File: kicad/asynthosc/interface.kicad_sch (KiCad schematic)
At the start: 22 parts, among them SW6 RotaryEncoder_Switch, SW7 SW_MEC_5G_LED, SW8 SW_MEC_5G_LED

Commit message: bom: adding jlc ref to generic
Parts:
- C51, C52: LCSC (none) -> C307331
- C53: LCSC (none) -> C377773
- C54, C55: LCSC (none) -> C28323
- C56: LCSC (none) -> C1779
- C57: LCSC (none) -> C49678
- R76, R77, R78, R79, R84: LCSC (none) -> C25744
- R80, R81: LCSC (none) -> C144055
- R82: LCSC (none) -> C26083
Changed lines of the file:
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@@
 			)
 		)
-		(property "LCSC" ""
+		(property "LCSC" "C1779"
 			(at 191.77 34.29 0)
 			(effects
@@
 			)
 		)
-		(property "LCSC" ""
+		(property "LCSC" "C307331"
 			(at 36.83 134.62 0)
 			(effects
@@
 			)
 		)
-		(property "LCSC" ""
+		(property "LCSC" "C49678"
 			(at 204.47 34.29 0)
 			(effects
@@
 			)
 		)
-		(property "LCSC" ""
+		(property "LCSC" "C28323"
 			(at 167.64 34.29 0)
 			(effects
@@
 			)
 		)
-		(property "LCSC" ""
+		(property "LCSC" "C25744"
 			(at 50.8 67.31 0)
 			(effects
@@
 			)
 		)
-		(property "LCSC" ""
+		(property "LCSC" "C377773"
 			(at 151.13 128.27 0)
 			(effects
@@
 			)
 		)
-		(property "LCSC" ""
+		(property "LCSC" "C25744"
 			(at 36.83 114.3 0)
 			(effects
@@
 			)
 		)
-		(property "LCSC" ""
+		(property "LCSC" "C25744"
 			(at 44.45 114.3 0)
 			(effects
@@
 			)
 		)
-		(property "LCSC" ""
+		(property "LCSC" "C25744"
 			(at 78.74 134.62 0)
 			(effects
@@
 			)
 		)
-		(property "LCSC" ""
+		(property "LCSC" "C144055"
 			(at 78.74 176.53 0)
 			(effects
@@
 			)
 		)
-		(property "LCSC" ""
+		(property "LCSC" "C25744"
 			(at 52.07 168.91 0)
 			(effects
@@
 			)
 		)
-		(property "LCSC" ""
+		(property "LCSC" "C26083"
 			(at 137.16 125.73 0)
 			(effects
@@
 			)
 		)
-		(property "LCSC" ""
+		(property "LCSC" "C28323"
 			(at 158.75 34.29 0)
 			(effects
@@
 			)
 		)
-		(property "LCSC" ""
+		(property "LCSC" "C307331"
 			(at 44.45 134.62 0)
 			(effects
@@
 			)
 		)
-		(property "LCSC" ""
+		(property "LCSC" "C144055"
 			(at 77.47 74.93 0)
 			(effects

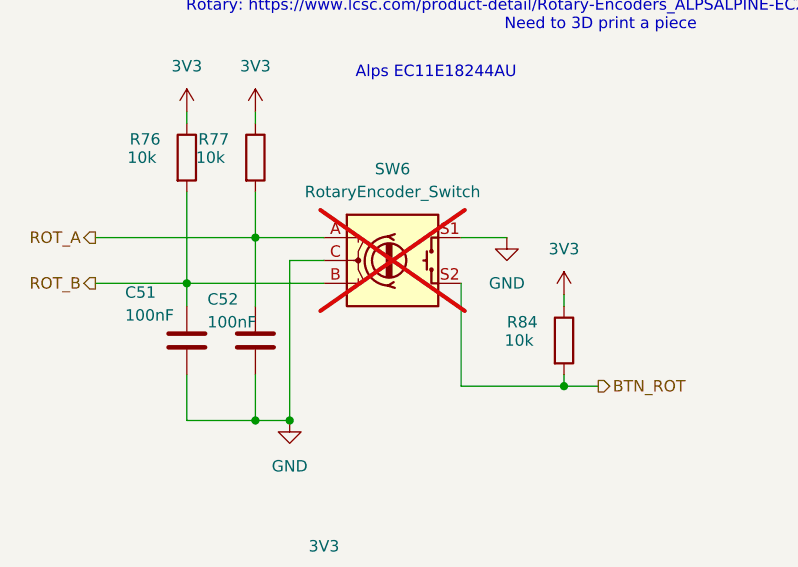
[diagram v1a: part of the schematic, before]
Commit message: sch: bom: fix footprints and bom
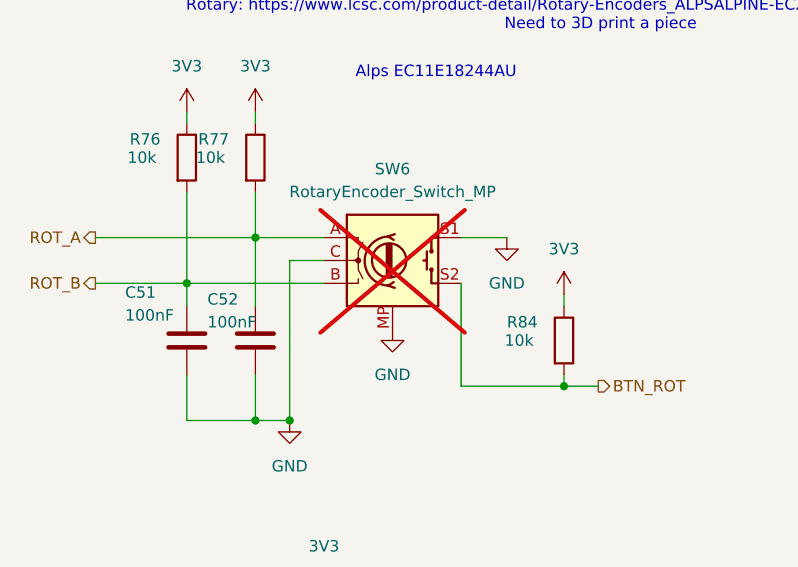
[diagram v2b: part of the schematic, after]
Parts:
- DS1: footprint asynthosc:Hirose_FH52-24S-0.5SH_1x24-1MP_P0.5mm_Horizontal -> Display:OLED-128O064D
- SW6: value RotaryEncoder_Switch -> RotaryEncoder_Switch_MP; symbol Device:RotaryEncoder_Switch -> Device:RotaryEncoder_Switch_MP
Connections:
- net GND: now also SW6.MP
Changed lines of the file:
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@@
 			)
 		)
-		(property "Footprint" "asynthosc:Hirose_FH52-24S-0.5SH_1x24-1MP_P0.5mm_Horizontal"
+		(property "Footprint" "Display:OLED-128O064D"
 			(at 183.642 96.774 0)
 			(effects
@@
 	)
 	(symbol
+		(lib_id "power:GND")
+		(at 59.69 133.35 0)
+		(unit 1)
+		(exclude_from_sim no)
+		(in_bom yes)
+		(on_board yes)
+		(dnp no)
+		(fields_autoplaced yes)
+		(property "Reference" "#PWR0162"
+			(at 59.69 139.7 0)
+			(effects
+				(font
+					(size 1.27 1.27)
+				)
+				(hide yes)
+			)
+		)
+		(property "Value" "GND"
+			(at 59.69 138.43 0)
+			(effects
+				(font
+					(size 1.27 1.27)
+				)
+			)
+		)
+		(property "Footprint" ""
+			(at 59.69 133.35 0)
+			(effects
+				(font
+					(size 1.27 1.27)
+				)
+				(hide yes)
+			)
+		)
+		(property "Datasheet" ""
+			(at 59.69 133.35 0)
+			(effects
+				(font
+					(size 1.27 1.27)
+				)
+				(hide yes)
+			)
+		)
+		(property "Description" "Power symbol creates a global label with name \"GND\" , ground"
+			(at 59.69 133.35 0)
+			(effects
+				(font
+					(size 1.27 1.27)
+				)
+				(hide yes)
+			)
+		)
+		(pin "1"
+		)
+		(instances
+			(project "asynthosc"
+				(path "/d73e377a-a016-415f-8824-91cc6e4907b9/b863f609-74bc-4dca-9f89-b76b25b90e2d"
+					(reference "#PWR0162")
+					(unit 1)
+				)
+			)
+		)
+	)
+	(symbol
 		(lib_id "power:+3V3")
 		(at 50.8 60.96 0)
@@
 	)
 	(symbol
-		(lib_id "Device:RotaryEncoder_Switch")
+		(lib_id "Device:RotaryEncoder_Switch_MP")
 		(at 59.69 125.73 0)
 		(unit 1)
@@
 			)
 		)
-		(property "Value" "RotaryEncoder_Switch"
+		(property "Value" "RotaryEncoder_Switch_MP"
 			(at 59.69 118.11 0)
 			(effects
@@
 		)
 		(property "Datasheet" "~"
-			(at 59.69 119.126 0)
-			(effects
-				(font
-					(size 1.27 1.27)
-				)
-				(hide yes)
-			)
-		)
-		(property "Description" "Rotary encoder, dual channel, incremental quadrate outputs, with switch"
-			(at 59.69 125.73 0)
+			(at 59.69 138.43 0)
+			(effects
+				(font
+					(size 1.27 1.27)
+				)
+				(hide yes)
+			)
+		)
+		(property "Description" "Rotary encoder, dual channel, incremental quadrate outputs, with switch and MP Pin"
+			(at 59.69 140.97 0)
 			(effects
 				(font
@@
 		(pin "S1"
 		)
-		(instances
+		(pin "MP"
+		)
+		(instances

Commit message: fix: footprint: button is polarized, fix led according to easyeda footprint
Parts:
- DS1: footprint Display:OLED-128O064D -> asynthosc:Hirose_FH52-24S-0.5SH_1x24-1MP_P0.5mm_Horizontal
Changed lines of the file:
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@@
 			)
 		)
-		(property "Footprint" "Display:OLED-128O064D"
+		(property "Footprint" "asynthosc:Hirose_FH52-24S-0.5SH_1x24-1MP_P0.5mm_Horizontal"
 			(at 183.642 96.774 0)
 			(effects

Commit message: sch: update bom
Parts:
- C57: value 100nF 25V X7R -> 100nF
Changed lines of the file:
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@@
 			)
 		)
-		(property "Value" "100nF 25V X7R"
-			(at 200.66 39.37 90)
+		(property "Value" "100nF"
+			(at 200.66 36.83 90)
 			(effects
 				(font
